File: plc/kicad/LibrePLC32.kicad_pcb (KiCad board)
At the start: 4 copper layers, 256 parts, among them CN1 DB128V-5.08-2P-GN-S, CN10 DB128V-5.08-6P-GN-S, CN11 DB2ERC-5.08-4P, CN12 DB2ERC-5.08-4P, CN2 DB128V-5.08-2P-GN-S, CN3 DB128V-5.08-2P-GN-S, CN4 DB128V-5.08-2P-GN-S, CN5 DB128V-5.08-2P-GN-S, CN6 DB128V-5.08-2P-GN-S, CN7 DB128V-5.08-2P-GN-S, CN8 DB128V-5.08-2P-GN-S, CN9 DB128V-5.08-2P-GN-S, J2 Conn_01x04_Pin, Q1 AO3400A, Q2 AO3400A, Q3 L8050QLT1G, Q4 L8050QLT1G, Q5 BSS138LT1G, Q6 CSD19537Q3, SW1 TSD003B08026A03, SW2 TSD003B08026A03, SW3 TSD003B08026A03, SW4 MSK12C02, SW5 MSK12C02, U1 TCA9535PWR, U10 ESP32-S3-MINI-1U, U11 BS-0601-SK-4W, U12 AHT20_C2757850, U13 CP2102N-A02-GQFN28R, U14 LMR16006XDDCR, U15 TPS54560DDAR, U16 TPS26630RGER, U17 TLV76733DRVR, U18 TCAN337DR, U19 THVD1450DR, U2 TPS272C45DRHFR, U20 W5500, U3 TPS272C45DRHFR, U4 ADS1115IDGSR, U5 LTV-814S-TA1-A, U6 LTV-814S-TA1-A, U7 LTV-814S-TA1-A, U8 LTV-814S-TA1-A, U9 RV-3028-C7, X1 X322525MRB4SI

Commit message: Removed CAN FLT resistor
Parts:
- removed R66: 100k, Resistor_SMD:R_0603_1608Metric
- removed R68: 3.09k, Resistor_SMD:R_0603_1608Metric
- removed U17: TLV76733DRVR, LibrePLC32:WSON-6_L2.0-W2.0-P0.65-TL-EP
- added C56: 100n, Capacitor_SMD:C_0603_1608Metric, F.Cu at (50.3, 162.1)
- added C57: 10u, Capacitor_SMD:C_0603_1608Metric, F.Cu at (74.0, 162.1)
- added Card1: TF PUSH, LibrePLC32:TF-SMD_TF-PUSH, F.Cu at (61.2, 167.4)
- added D19: LED, LED_SMD:LED_0805_2012Metric, F.Cu at (54.6, 179.2)
- added D20: LED, LED_SMD:LED_0805_2012Metric, F.Cu at (54.6, 182.3)
- added J3: Conn_01x02_Pin, Connector_PinSocket_2.54mm:PinSocket_1x02_P2.54mm_Vertical, F.Cu at (437.8, 193.0)
- added R100: 10k, Resistor_SMD:R_0603_1608Metric, F.Cu at (50.3, 172.1)
- added R101: 470, Resistor_SMD:R_0603_1608Metric, F.Cu at (50.3, 174.6)
- added R102: 10k, Resistor_SMD:R_0603_1608Metric, F.Cu at (50.3, 177.1)
- added R103: 470, Resistor_SMD:R_0603_1608Metric, F.Cu at (50.3, 179.6)
- added R104: 470, Resistor_SMD:R_0603_1608Metric, F.Cu at (50.3, 182.1)
- added R105: 3.01k, Resistor_SMD:R_0603_1608Metric, F.Cu at (74.0, 164.6)
- added R106: 11.8k, Resistor_SMD:R_0603_1608Metric, F.Cu at (74.0, 167.1)
- added R107: 3.74k, Resistor_SMD:R_0603_1608Metric, F.Cu at (74.0, 169.6)
- added R108: 50k, Resistor_SMD:R_0603_1608Metric, F.Cu at (74.0, 172.1)
- added R94: 10k, Resistor_SMD:R_0603_1608Metric, F.Cu at (436.5, 184.1)
- added R95: 0, Resistor_SMD:R_0603_1608Metric, F.Cu at (69.4, 182.5)
- added R96: 0, Resistor_SMD:R_0603_1608Metric, F.Cu at (69.4, 185.0)
- added R97: 10k, Resistor_SMD:R_0603_1608Metric, F.Cu at (50.3, 164.6)
- added R98: 10k, Resistor_SMD:R_0603_1608Metric, F.Cu at (50.3, 167.1)
- added R99: 10k, Resistor_SMD:R_0603_1608Metric, F.Cu at (50.3, 169.6)
- added U21: TPS54560BDDAR, LibrePLC32:POWERPAD-SO-8_L4.9-W3.9-P1.27-LS6.0-BL-EP, F.Cu at (79.1, 165.1)
- C1, C2: value 1n -> 100p
- C19: value 100n -> 18u
- C37: value 100n -> 10u
- C39: value 1u -> 22u
- D18: value TS3314PLX -> LED; footprint LibrePLC32:SOT-23-5_L2.9-W1.6-P0.95-LS2.8-BR -> LED_SMD:LED_0805_2012Metric
- L1: value 22u -> 27u
- R10, R9: value 100 -> 10k
- R59: value 33.2k -> 28k
- R60: value 10k -> 8.2k
- R63: value 316k -> 383k
- R64: value 73.2k -> 56k
- R70: value 10k -> 12.4k
- R72: value 86.6k -> 499k
- R73: value 10k -> 55.44k
- U15: value TPS54560DDAR -> TPS7A5201QRGRRQ1; footprint LibrePLC32:SOIC-8_L5.0-W4.0-P1.27-LS6.0-BL-EP2.0 -> LibrePLC32:VQFN-20_L3.5-W3.5-P0.50-TL-EP
- moved C40 4.72 mm to (428.9, 178.9)
- moved C41 4.72 mm to (426.9, 178.9)
- moved CN11 4.72 mm to (446.3, 173.6)
- moved D15 4.72 mm to (441.4, 178.9)
- moved R80 4.72 mm to (442.2, 191.4)
- moved SW4 4.72 mm to (445.9, 190.9)
- moved U18 4.49 mm to (434.1, 178.9)
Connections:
- net /Ethernet/ETH_MISO renamed /Ethernet/SPI_MISO
- net /Ethernet/ETH_MOSI renamed /Ethernet/SPI_MOSI
- net /Ethernet/ETH_SCLK renamed /Ethernet/SPI_SCLK
- net Net-(U10-IO2) renamed /MCU/S_LED0
- net Net-(U10-IO3) renamed /MCU/S_LED1
- net Net-(U10-IO6) renamed /MCU/SD_CS
- C20 pad 1: Net-(U15-VIN) -> Net-(U21-VIN)
- C23 pad 1: Net-(U15-VIN) -> Net-(U21-VIN)
- C24 pad 1: Net-(U15-VIN) -> Net-(U21-VIN)
- C26 pad 1: Net-(U15-VIN) -> Net-(U21-VIN)
- C29 pad 1: Net-(U15-BOOT) -> Net-(U21-BOOT)
- C33 pad 2: Net-(U15-COMP) -> Net-(U21-COMP)
- D17 pad 1: /Ethernet/ETH_TX+ -> /Ethernet/RJ45_RX-
- D17 pad 3: /Ethernet/ETH_TX- -> /Ethernet/RJ45_TX-
- D17 pad 4: /Ethernet/RJ45_TX- -> /Ethernet/RJ45_RX+
- D18 pad 1: /Ethernet/ETH_RX+ -> GND
- D18 pad 2: GND -> Net-(D18-A)
- F2 pad 1: Net-(U15-VIN) -> Net-(U21-VIN)
- R61 pad 1: Net-(U15-VIN) -> Net-(U21-VIN)
- R61 pad 2: Net-(U15-EN) -> Net-(U21-EN)
- R62 pad 1: Net-(U15-EN) -> Net-(U21-EN)
- R67 pad 1: Net-(U15-RT/CLK) -> Net-(U21-RT/CLK)
- R71 pad 1: Net-(U15-COMP) -> Net-(U21-COMP)
- TP7 pad 1: Net-(U10-IO7) -> GND
- U10 pad 11: Net-(U10-IO7) -> GND
- U14 pad 4: Net-(U14-SHDN) -> unconnected-(U14-SHDN-Pad4)
- U15 pad 1: Net-(U15-BOOT) -> +3V3
- U15 pad 2: Net-(U15-VIN) -> unconnected-(U15-NC-Pad2)
- U15 pad 3: Net-(U15-EN) -> /Power/MAIN_FB
- U15 pad 4: Net-(U15-RT/CLK) -> /Power/MAIN_PG
- U15 pad 5: /Power/FB -> unconnected-(U15-DNC-Pad5)
- U15 pad 6: Net-(U15-COMP) -> unconnected-(U15-NC-Pad6)
- U15 pad 7: GND -> unconnected-(U15-NC-Pad7)
- U15 pad 8: Net-(D8-K) -> GND
- U15 pad 9: GND -> unconnected-(U15-NC-Pad9)
- U18 pad 1: /CAN/CAN_TX -> Net-(U18-TXD)
- U18 pad 4: /CAN/CAN_RX -> Net-(U18-RXD)
- U20 pad 1: /Ethernet/ETH_TX- -> /Ethernet/RJ45_TX-
- U20 pad 2: /Ethernet/ETH_TX+ -> /Ethernet/RJ45_TX+
- U20 pad 5: /Ethernet/ETH_RX- -> /Ethernet/RJ45_RX-
- U20 pad 6: /Ethernet/ETH_RX+ -> /Ethernet/RJ45_RX+
- U4 pad 4: /Terminal Blocks Interface/T1_SNS -> /Terminal Blocks Interface/T1_ADC
- U4 pad 5: /Terminal Blocks Interface/T2_SNS -> /Terminal Blocks Interface/T2_ADC
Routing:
- net /CAN/CAN_L: track 0.00 -> 14.8 mm
- net /CAN/CAN_H: track 0.00 -> 10.0 mm

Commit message: Added more wiring
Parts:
- moved R84 4.19 mm to (426.1, 99.8)
- moved R83 2.40 mm to (435.8, 102.8)
- moved R82 2.40 mm to (435.9, 105.2)
- moved C42 1.60 mm to (433.0, 100.2)
- moved R85 0.91 mm to (422.9, 104.0)
- moved CN12 0.54 mm to (444.6, 99.0)
- moved J3 0.30 mm to (437.8, 192.7)
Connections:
- CN12 pad 3: /RS-485/EXT_RS485_A -> /RS-485/EXT_RS485_B
- CN12 pad 4: /RS-485/EXT_RS485_B -> /RS-485/EXT_RS485_A
- D16 pad 1: /RS-485/EXT_RS485_A -> /RS-485/EXT_RS485_B
- D16 pad 2: /RS-485/EXT_RS485_B -> /RS-485/EXT_RS485_A
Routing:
- net /RS-485/EXT_RS485_B: track 0.00 -> 28.7 mm, vias 0 -> 1
- net /CAN/CAN_H: track 10.0 -> 35.6 mm, vias 0 -> 1
- net /RS-485/EXT_RS485_A: track 0.00 -> 22.5 mm
- net /CAN/CAN_L: track 14.8 -> 27.9 mm, vias 0 -> 1
- net GND: track 0.00 -> 12.4 mm, vias 0 -> 12
- net /RS-485/RS485_DIR: track 0.00 -> 10.6 mm
- net /RS-485/RS485_RXD: track 0.00 -> 8.74 mm
- net /RS-485/RS485_TXD: track 0.00 -> 7.26 mm
- net +3V3: track 0.00 -> 5.79 mm, vias 0 -> 1
- net Net-(U19-A): track 0.00 -> 3.77 mm
- net Net-(U19-B): track 0.00 -> 3.75 mm
- added copper zone on F.Cu, net +3V3
- added copper zone on F.Cu, net GND

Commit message: Added TPS54560 PCB placement
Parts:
- removed D1: SMBJ36A, LibrePLC32:SMB_L4.6-W3.6-LS5.3-RD
- removed L2: 7.2u, Inductor_SMD:L_1206_3216Metric
- added L4: 7.2u, LibrePLC32:IND-SMD_3P-L13.5-W13.0-P6.9, F.Cu at (15.2, 476.6)
- moved F2 411.4 mm to (-13.8, 482.4), turned to 90 degrees
- moved R67 400.9 mm to (-4.70, 487.4), turned to -90 degrees
- moved TP21 400.0 mm to (4.80, 467.4)
- moved TP22 399.9 mm to (-0.60, 468.5)
- moved R75 398.2 mm to (13.9, 485.5), turned to -90 degrees
- moved R76 397.0 mm to (10.9, 485.5), turned to 90 degrees
- moved C20 394.0 mm to (-9.50, 483.1), turned to 90 degrees
- moved R62 393.0 mm to (-11.1, 487.8), turned to -90 degrees
- moved R61 392.4 mm to (-11.1, 484.7), turned to -90 degrees
- moved C30 391.2 mm to (8.80, 485.6), turned to -90 degrees
- moved C29 391.2 mm to (4.40, 481.4)
- moved R71 387.2 mm to (6.50, 487.3)
- moved C23 386.4 mm to (-7.81, 483.1), turned to 90 degrees
- moved C33 384.5 mm to (5.70, 484.8), turned to -90 degrees
- moved C24 383.5 mm to (-6.20, 483.1), turned to 90 degrees
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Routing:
- net 5V: track 0.00 -> 47.7 mm
- net Net-(D8-K): track 0.00 -> 25.9 mm
- net GND: track 12.4 -> 36.4 mm, vias 12 -> 25
- net /Power/FB: track 0.00 -> 12.4 mm
- net Net-(U21-VIN): track 0.00 -> 10.7 mm
- net Net-(U21-EN): track 0.00 -> 10.0 mm
- net Net-(U21-BOOT): track 0.00 -> 7.23 mm, vias 0 -> 2
- net Net-(U21-COMP): track 0.00 -> 4.24 mm
- net Net-(U21-RT/CLK): track 0.00 -> 2.08 mm
- net Net-(D9-K): track 0.00 -> 1.96 mm
- net Net-(C30-Pad2): track 0.00 -> 1.96 mm

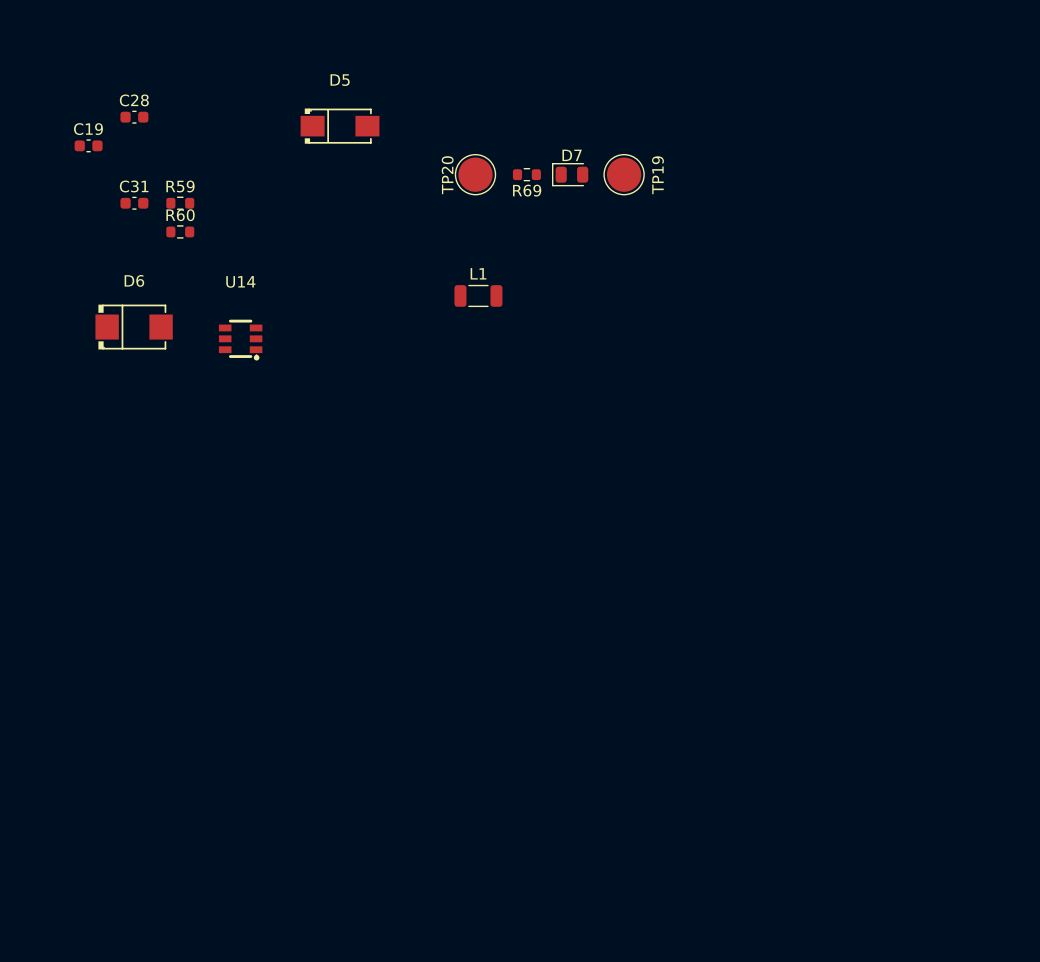
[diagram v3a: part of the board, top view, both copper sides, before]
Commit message: LMR16006X PCB placement
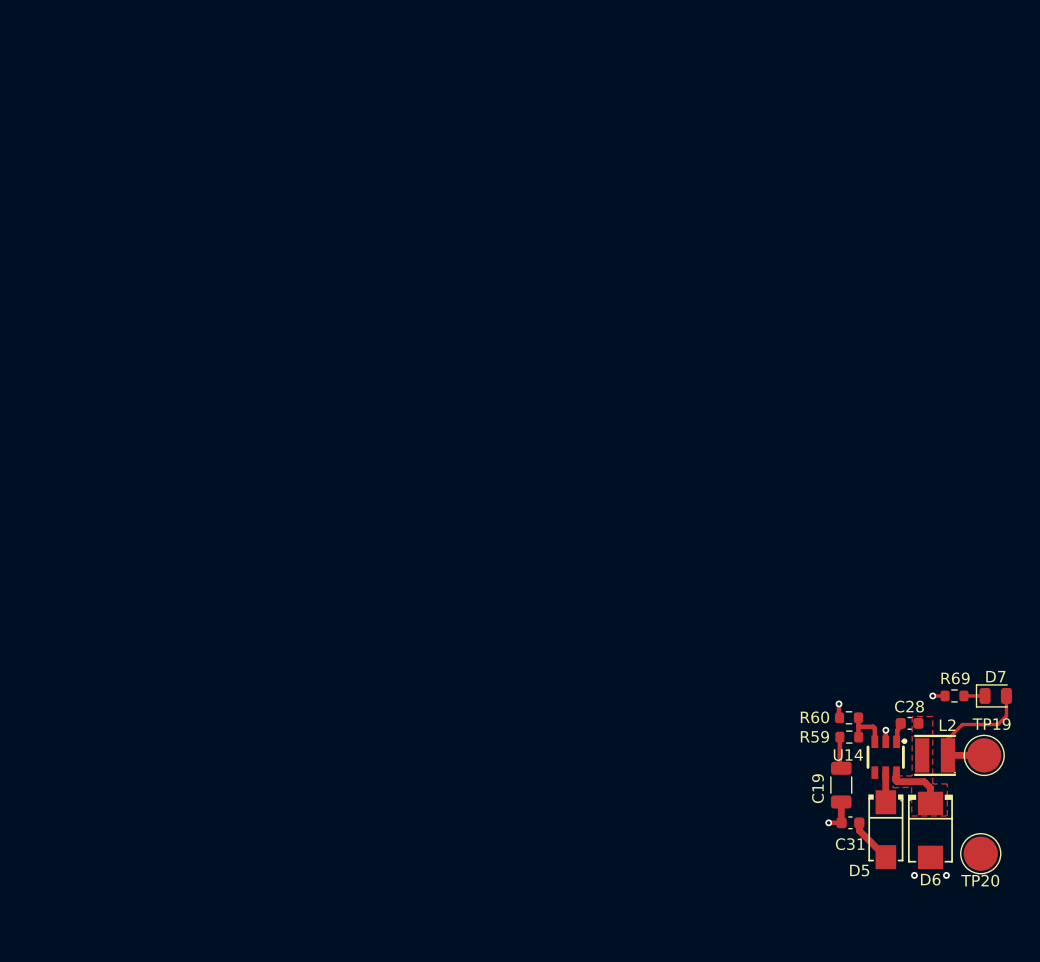
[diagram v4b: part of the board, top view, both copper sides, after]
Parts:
- removed L1: 27u, Inductor_SMD:L_1206_3216Metric
- added L2: 27u, LibrePLC32:IND-SMD_L3.5-W3.0_SLF0302, F.Cu at (453.7, 393.8)
- C19: value 18u -> 2.2u; footprint Capacitor_SMD:C_0603_1608Metric -> Capacitor_SMD:C_1206_3216Metric
- R60: value 8.2k -> 8.45k
- moved C19 86.4 mm to (445.5, 396.4), turned to -90 degrees
- moved C28 86.1 mm to (451.5, 391.0)
- moved C31 82.8 mm to (446.3, 399.7)
- moved D6 82.4 mm to (453.3, 400.4), turned to -90 degrees
- moved D5 77.9 mm to (449.4, 400.3), turned to -90 degrees
- moved R59 74.9 mm to (446.2, 392.2)
- moved TP20 74.0 mm to (457.7, 402.4), turned to 180 degrees
- moved R60 72.3 mm to (446.2, 390.5), turned to 180 degrees
- moved U14 67.3 mm to (449.4, 394.0), turned to 90 degrees
- moved TP19 59.8 mm to (458.0, 393.8)
- moved R69 59.0 mm to (455.4, 388.6)
- moved D7 58.8 mm to (459.0, 388.6)
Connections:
- C19 pad 1: GND -> +3V3_AUX
- C19 pad 2: +3V3_AUX -> GND
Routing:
- net +3V3_AUX: track 0.00 -> 14.7 mm
- net GND: track 36.4 -> 42.7 mm, vias 25 -> 31
- net Net-(D6-K): track 0.00 -> 5.32 mm
- net Net-(U14-FB): track 0.00 -> 4.37 mm
- net /Power/V_IN_MAIN: track 0.00 -> 3.96 mm
- net Net-(D5-C): track 0.00 -> 2.60 mm
- net Net-(D7-K): track 0.00 -> 1.85 mm
- net Net-(U14-CB): track 0.00 -> 1.76 mm
- added copper zone on F.Cu, net +3V3_AUX

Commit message: TPS26630 PCB placement
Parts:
- C18, C21: footprint Capacitor_SMD:C_0603_1608Metric -> Capacitor_SMD:C_Elec_10x10.2
- C22: value 1u -> 2.2u; footprint Capacitor_SMD:C_0603_1608Metric -> Capacitor_SMD:C_1206_3216Metric
- moved C21 679.1 mm to (-354.8, 461.8), turned to 90 degrees
- moved Q5 640.9 mm to (-366.8, 471.2), turned to 180 degrees
- moved Q6 639.4 mm to (-363.6, 468.8), turned to -90 degrees
- moved U16 628.6 mm to (-358.5, 471.1)
- moved R65 628.6 mm to (-361.4, 475.1), turned to 90 degrees
- moved D4 624.7 mm to (-368.5, 462.5), turned to -90 degrees
- moved R70 616.7 mm to (-355.6, 475.1), turned to -90 degrees
- moved R78 616.1 mm to (-350.2, 471.0), turned to -90 degrees
- moved R64 615.3 mm to (-363.0, 475.1), turned to -90 degrees
- moved R63 615.0 mm to (-363.0, 472.1), turned to -90 degrees
- moved R77 613.3 mm to (-342.6, 474.4), turned to -90 degrees
- moved R72 609.8 mm to (-353.4, 471.0), turned to -90 degrees
- moved R73 608.0 mm to (-351.8, 472.7), turned to -90 degrees
- moved C22 608.0 mm to (-363.9, 462.5), turned to -90 degrees
- moved C27 605.2 mm to (-358.8, 475.1), turned to 90 degrees
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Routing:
- net /Power/~{PPIC_SHDN}: track 0.00 -> 18.8 mm
- net /Power/V_IN_MAIN: track 3.96 -> 12.2 mm
- net /Power/PPIC_DRV: track 0.00 -> 8.10 mm, vias 0 -> 2
- net /Power/PPIC_BGATE: track 0.00 -> 7.29 mm
- net GND: track 42.7 -> 49.9 mm, vias 31 -> 44
- net /Power/PPIC_PGOOD: track 0.00 -> 6.77 mm
- net /Power/PPIC_OVP: track 0.00 -> 5.77 mm
- net /Power/PPIC_PGTH: track 0.00 -> 4.98 mm
- net /Power/PPIC_UVLO: track 0.00 -> 4.15 mm
- net /Power/PPIC_IMON: track 0.00 -> 2.58 mm
- net /Power/PPIC_ILIM: track 0.00 -> 1.99 mm
- net /Power/PPIC_dVdT: track 0.00 -> 1.28 mm
- added copper zone on F.Cu, net /Power/PPIC_BGATE
- added copper zone on F.Cu, net /Power/PPIC_IN
- added copper zone on F.Cu, net /Power/V_IN_MAIN
- added copper zone on F.Cu, net V_FIELD

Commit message: TPS7A52-Q1 PCB placement
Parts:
- C37: value 10u -> 22u
- moved C39 302.0 mm to (261.6, 396.6), turned to -90 degrees
- moved C37 299.2 mm to (249.8, 395.7), turned to -90 degrees
- moved C38 299.1 mm to (260.1, 396.6), turned to -90 degrees
- moved R106 293.5 mm to (256.9, 396.6), turned to 90 degrees
- moved C57 291.3 mm to (248.0, 395.7), turned to -90 degrees
- moved R107 291.3 mm to (258.4, 395.0), turned to 90 degrees
- moved D14 291.0 mm to (268.9, 392.6)
- moved R79 289.8 mm to (265.6, 392.6), turned to 180 degrees
- moved R108 287.2 mm to (256.9, 393.5), turned to 90 degrees
- moved U15 275.2 mm to (253.5, 395.9), turned to 180 degrees
- moved TP23 261.0 mm to (264.9, 397.6)
- moved TP28 250.6 mm to (261.9, 392.5)
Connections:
- C32 pad 2: 5V -> +5V
- C34 pad 2: 5V -> +5V
- C35 pad 2: 5V -> +5V
- C37 pad 2: 5V -> +5V
- D10 pad 1: +5V -> ++5V
- D11 pad 1: +5V -> ++5V
- D2 pad 1: +5V -> ++5V
- D3 pad 1: +5V -> ++5V
- D9 pad 2: 5V -> +5V
- L4 pad 2: 5V -> +5V
- R75 pad 1: 5V -> +5V
- RLY1 pad 4: +5V -> ++5V
- RLY2 pad 4: +5V -> ++5V
- TP21 pad 1: 5V -> +5V
- U15 pad 14: 5V -> +5V
- U15 pad 15: 5V -> +5V
- U15 pad 16: 5V -> +5V
- U15 pad 17: 5V -> +5V
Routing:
- net +5V: track 0.00 -> 52.8 mm
- net 5V: track 47.7 -> 0.00 mm
- net +3V3: track 5.79 -> 21.1 mm, vias 1 -> 3
- net GND: track 49.9 -> 63.0 mm, vias 44 -> 56
- net Net-(U15-NR/SS): track 0.00 -> 4.20 mm
- net /Power/MAIN_FB: track 0.00 -> 3.27 mm
- net /Power/MAIN_PG: track 0.00 -> 2.16 mm
- net Net-(D14-K): track 0.00 -> 1.58 mm
- added copper zone on F.Cu, net +5V

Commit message: Updated W5500 to reference schematic
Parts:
- moved D18 175.7 mm to (73.5, 111.1)
- moved C52 74.5 mm to (176.0, -84.8), turned to 90 degrees
- moved C54 66.9 mm to (172.2, -80.0), turned to 180 degrees
- moved C49 66.4 mm to (172.3, -81.8), turned to 180 degrees
- moved C53 66.2 mm to (177.8, -84.8), turned to 90 degrees
- moved C47 64.7 mm to (188.0, -78.5), turned to 0 degrees
- moved C43 63.8 mm to (175.6, -68.0), turned to -90 degrees
- moved X1 60.8 mm to (178.8, -67.7), turned to 0 degrees
- moved C48 59.4 mm to (186.5, -82.5)
- moved C44 58.4 mm to (182.1, -68.0), turned to -90 degrees
- moved R101 57.8 mm to (74.2, 122.0)
- moved L3 57.7 mm to (188.2, -76.5)
- moved R86 56.9 mm to (178.8, -64.5), turned to 0 degrees
- moved U20 56.9 mm to (180.2, -77.8)
- moved R87 51.2 mm to (172.2, -83.5), turned to 180 degrees
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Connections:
- D17 pad 3: /Ethernet/RJ45_TX- -> /Ethernet/RJ45_RX+
- D17 pad 4: /Ethernet/RJ45_RX+ -> /Ethernet/RJ45_TX+
- D17 pad 5: /Ethernet/RJ45_TX+ -> /Ethernet/RJ45_TX-
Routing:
- net +3V3A: track 0.00 -> 49.4 mm, vias 0 -> 4
- net Net-(RJ1-LED(G)_K): track 0.00 -> 43.8 mm
- net Net-(RJ1-LED(Y)_K): track 0.00 -> 38.1 mm, vias 0 -> 1
- net +3V3: track 21.1 -> 42.8 mm
- net /Ethernet/RJ45_RX+: track 0.00 -> 17.9 mm
- net /Ethernet/RJ45_TX+: track 0.00 -> 17.8 mm
- net /Ethernet/RJ45_RX-: track 0.00 -> 17.8 mm
- net /Ethernet/RJ45_TX-: track 0.00 -> 17.7 mm
- net /Ethernet/ETH_XO: track 0.00 -> 12.6 mm
- net /Ethernet/ETH_XI: track 0.00 -> 12.4 mm
- net /Ethernet/~{ETH_CS}: track 0.00 -> 8.30 mm
- net /Ethernet/ETH_EXPRES: track 0.00 -> 7.42 mm
- net /Ethernet/ETH_LED_G: track 0.00 -> 6.38 mm
- net GND: track 63.0 -> 69.0 mm, vias 56 -> 57
- net /Ethernet/~{ETH_INT}: track 0.00 -> 3.88 mm
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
